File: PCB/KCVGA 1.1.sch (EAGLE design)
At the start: 64 parts, among them IC1 XC3S50ATQ144, IC2 PIC32MX250F128, IC3 M68AW128MND, IC4 LD117AS12, IC5 LD117AS33, IC6 74245ADB, X1 D-SUB15, X3 MINI-USB

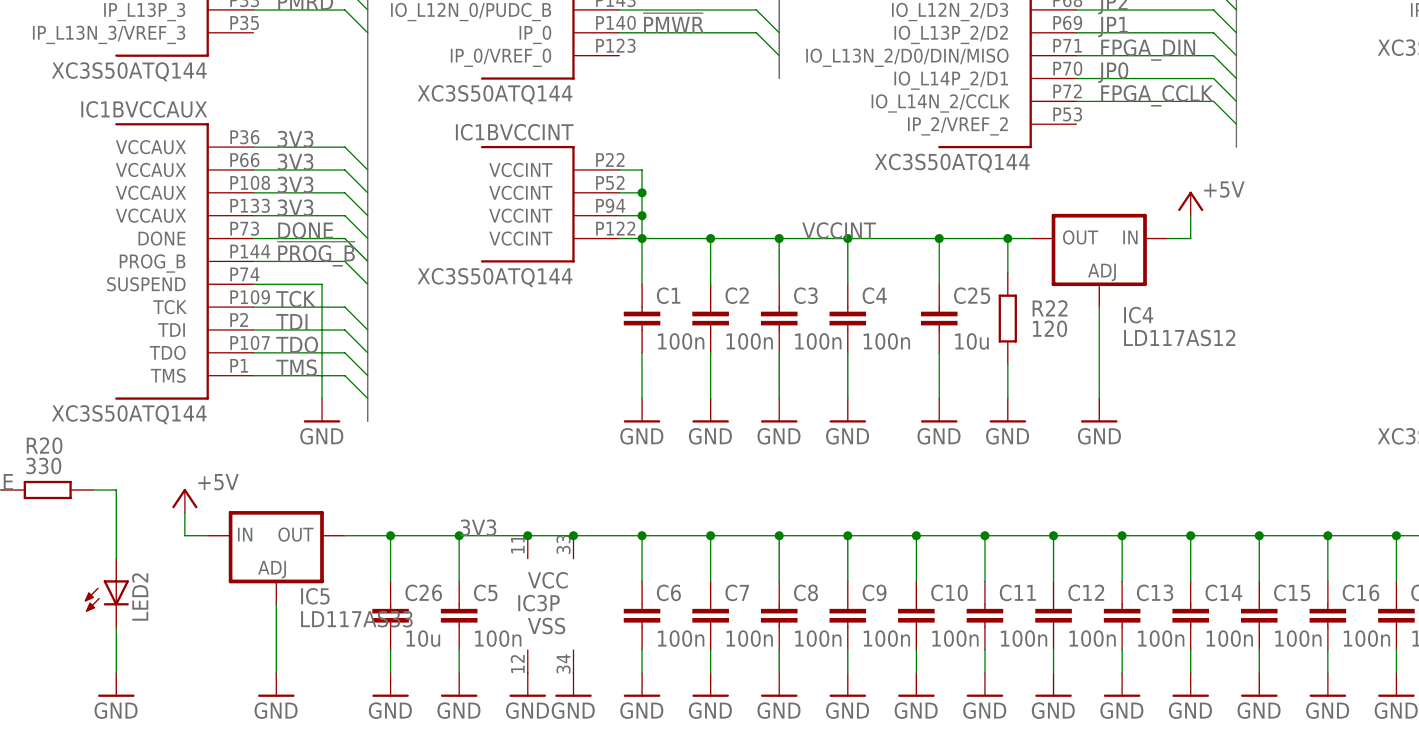
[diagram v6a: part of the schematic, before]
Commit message: optimized silkscreen
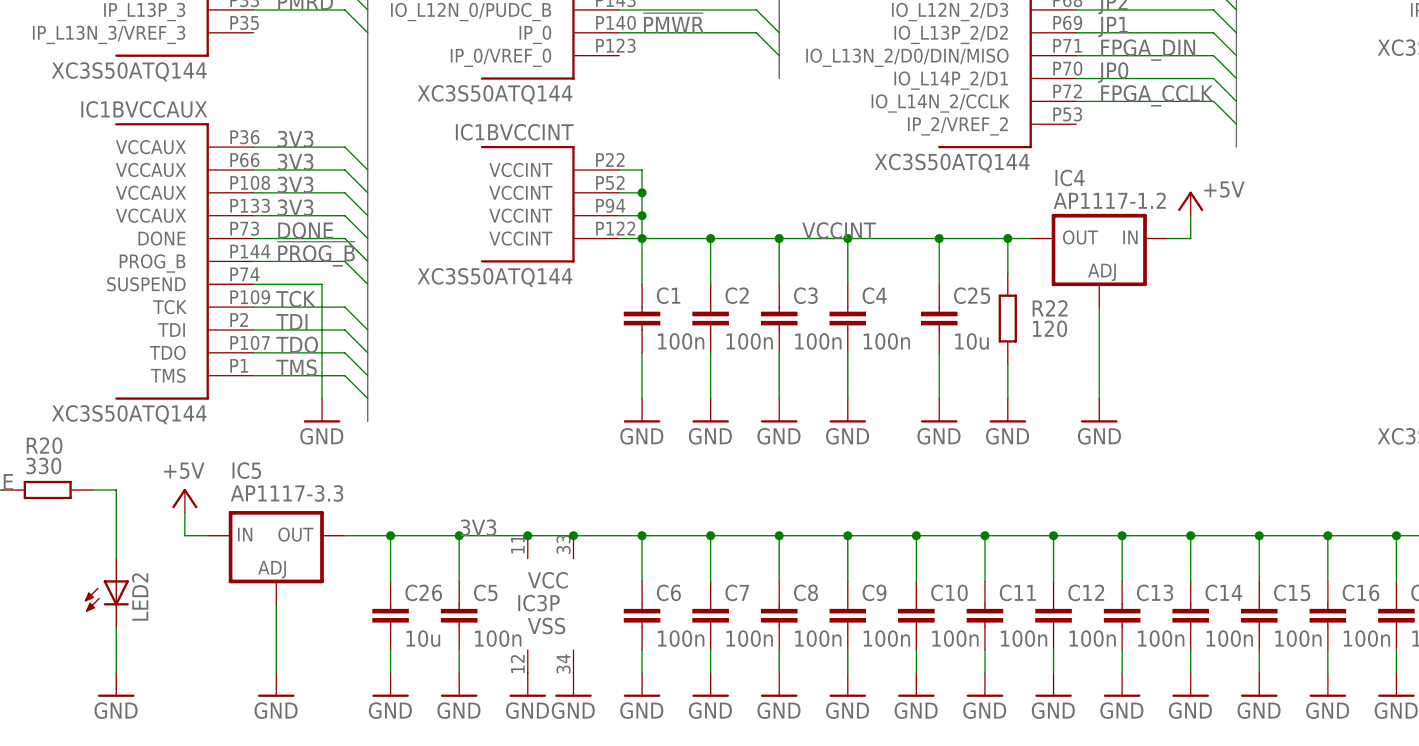
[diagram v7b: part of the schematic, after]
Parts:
- IC4: value LD117AS12 -> AP1117-1.2
- IC5: value LD117AS33 -> AP1117-3.3
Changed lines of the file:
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@@
 <part name="GND29" library="supply1" deviceset="GND" device=""/>
 <part name="X5" library="pinhead" deviceset="PINHD-1X6" device=""/>
-<part name="IC4" library="v-reg" deviceset="LD117A?*" device="S" technology="12TR" value="LD117AS12"/>
-<part name="IC5" library="v-reg" deviceset="LD117A?*" device="S" technology="33TR" value="LD117AS33"/>
+<part name="IC4" library="v-reg" deviceset="LD117A?*" device="S" technology="12TR" value="AP1117-1.2"/>
+<part name="IC5" library="v-reg" deviceset="LD117A?*" device="S" technology="33TR" value="AP1117-3.3"/>
 <part name="X2" library="pinhead" deviceset="PINHD-1X3" device=""/>
 <part name="P+2" library="supply1" deviceset="+5V" device=""/>
@@
 <instance part="X5" gate="A" x="177.8" y="83.82"/>
 <instance part="IC4" gate="G$1" x="93.98" y="-7.62" smashed="yes" rot="MR0">
-<attribute name="NAME" x="96.52" y="-15.24" size="1.778" layer="95" rot="MR180"/>
-<attribute name="VALUE" x="96.52" y="-17.78" size="1.778" layer="96" rot="MR180"/>
-</instance>
-<instance part="IC5" gate="G$1" x="2.54" y="-40.64"/>
+<attribute name="NAME" x="88.9" y="0" size="1.778" layer="95" rot="MR180"/>
+<attribute name="VALUE" x="88.9" y="-2.54" size="1.778" layer="96" rot="MR180"/>
+</instance>
+<instance part="IC5" gate="G$1" x="2.54" y="-40.64" smashed="yes">
+<attribute name="NAME" x="-2.54" y="-34.29" size="1.778" layer="95"/>
+<attribute name="VALUE" x="-2.54" y="-36.83" size="1.778" layer="96"/>
+</instance>
 <instance part="X2" gate="A" x="147.32" y="116.84" rot="R180"/>
 <instance part="P+2" gate="1" x="104.14" y="-2.54" smashed="yes" rot="MR0">
@@
 <instance part="GND31" gate="1" x="2.54" y="-58.42"/>
 <instance part="P+3" gate="1" x="-7.62" y="-35.56" smashed="yes">
-<attribute name="VALUE" x="-6.35" y="-35.56" size="1.778" layer="96"/>
+<attribute name="VALUE" x="-10.16" y="-34.29" size="1.778" layer="96"/>
 </instance>
 <instance part="GND32" gate="1" x="-68.58" y="99.06"/>
